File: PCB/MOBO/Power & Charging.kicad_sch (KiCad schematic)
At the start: 53 parts, among them J201 MAIN-USBC-OTG/PWR, Q201 AO3401A, Q202 FS8205A, Q203 IRLML6344, Q204 Si4435DDY, SW201 PCM12SMTR, U201 DW01A, U202 LC709203FQH-01TWG, U203 MCP73871-1AA, U204 TPS61230DRC

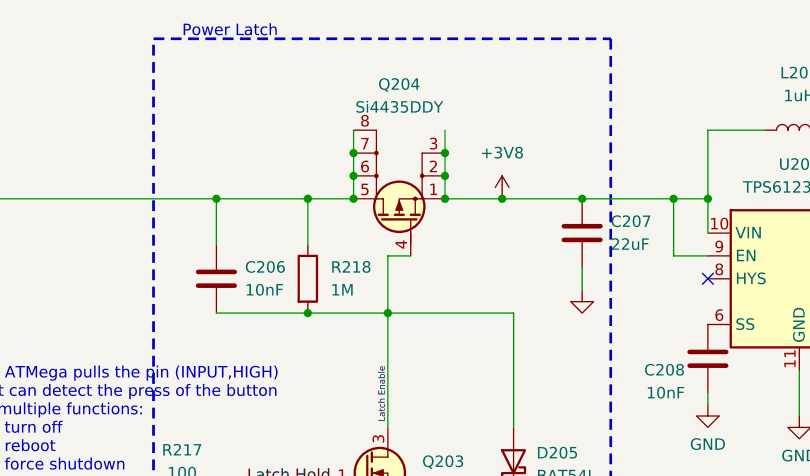
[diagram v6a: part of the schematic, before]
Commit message: replaced latching circuit PMOS
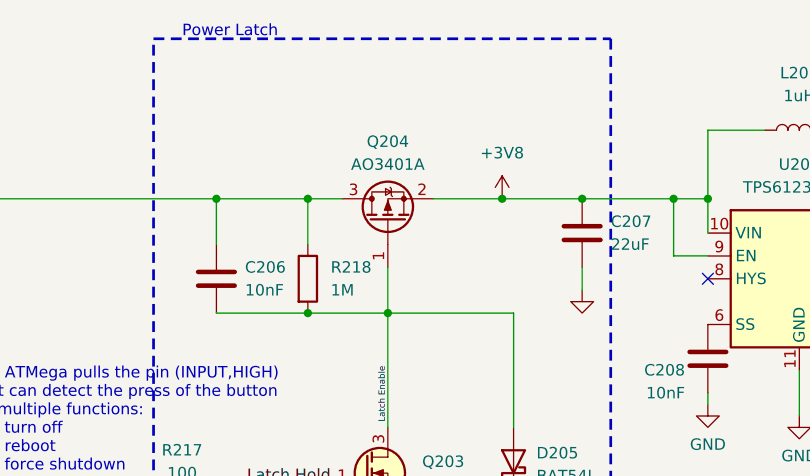
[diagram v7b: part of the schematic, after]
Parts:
- removed Q204: Si4435DDY, Package_SO:SOIC-8-1EP_3.9x4.9mm_P1.27mm_EP2.41x3.3mm, symbol PCM_Transistor_MOSFET_AKL:Si4435DDY
- added Q204: AO3401A, Package_TO_SOT_SMD:SOT-23, symbol Transistor_FET:AO3401A
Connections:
- net +3V8: now also Q204.2 (S)
- net Charger 3V8 out: now also Q204.3 (D)
- net Latch Enable: now also Q204.1 (G)
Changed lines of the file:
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@@
 	)
 	(junction
+		(at 252.73 36.83)
+		(diameter 0)
+		(color 0 0 0 0)
+	)
+	(junction
 		(at 340.36 43.18)
 		(diameter 0)
@@
 	)
 	(junction
-		(at 257.81 36.83)
-		(diameter 0)
-		(color 0 0 0 0)
-	)
-	(junction
 		(at 27.94 74.93)
 		(diameter 0)
@@
 	)
 	(junction
-		(at 274.32 36.83)
-		(diameter 0)
-		(color 0 0 0 0)
-	)
-	(junction
 		(at 63.5 36.83)
 		(diameter 0)
@@
 	)
 	(junction
-		(at 267.97 34.29)
-		(diameter 0)
-		(color 0 0 0 0)
-	)
-	(junction
 		(at 335.28 43.18)
 		(diameter 0)
@@
 	)
 	(junction
-		(at 267.97 36.83)
-		(diameter 0)
-		(color 0 0 0 0)
-	)
-	(junction
 		(at 242.57 36.83)
 		(diameter 0)
@@
 	)
 	(junction
-		(at 267.97 31.75)
-		(diameter 0)
-		(color 0 0 0 0)
-	)
-	(junction
 		(at 361.95 43.18)
 		(diameter 0)
@@
 	)
 	(junction
-		(at 257.81 31.75)
-		(diameter 0)
-		(color 0 0 0 0)
-	)
-	(junction
 		(at 134.62 96.52)
 		(diameter 0)
@@
 	)
 	(junction
-		(at 252.73 36.83)
-		(diameter 0)
-		(color 0 0 0 0)
-	)
-	(junction
 		(at 74.93 227.33)
 		(diameter 0)
@@
 	)
 	(junction
+		(at 274.32 36.83)
+		(diameter 0)
+		(color 0 0 0 0)
+	)
+	(junction
 		(at 260.35 85.09)
 		(diameter 0)
@@
 	)
 	(junction
-		(at 257.81 34.29)
-		(diameter 0)
-		(color 0 0 0 0)
-	)
-	(junction
 		(at 326.39 50.8)
 		(diameter 0)
@@
 	(wire
 		(pts
-			(xy 252.73 36.83) (xy 257.81 36.83)
-		)
-		(stroke
-			(width 0)
-			(type default)
-		)
-	)
-	(wire
-		(pts
 			(xy 62.23 36.83) (xy 63.5 36.83)
 		)
@@
 	(wire
 		(pts
-			(xy 261.62 43.18) (xy 261.62 49.53)
-		)
-		(stroke
-			(width 0)
-			(type default)
-		)
-	)
-	(wire
-		(pts
 			(xy 128.27 96.52) (xy 134.62 96.52)
 		)
@@
 	(wire
 		(pts
-			(xy 267.97 29.21) (xy 267.97 31.75)
-		)
-		(stroke
-			(width 0)
-			(type default)
-		)
-	)
-	(wire
-		(pts
 			(xy 127 41.91) (xy 127 44.45)
 		)
@@
 	(wire
 		(pts
-			(xy 257.81 31.75) (xy 257.81 34.29)
-		)
-		(stroke
-			(width 0)
-			(type default)
-		)
-	)
-	(wire
-		(pts
 			(xy 139.7 210.82) (xy 147.32 210.82)
 		)
@@
 	(wire
 		(pts
-			(xy 261.62 43.18) (xy 264.16 43.18)
-		)
-		(stroke
-			(width 0)
-			(type default)
-		)
-	)
-	(wire
-		(pts
 			(xy 119.38 36.83) (xy 137.16 36.83)
 		)
@@
 	(wire
 		(pts
-			(xy 252.73 68.58) (xy 252.73 71.12)
+			(xy 266.7 36.83) (xy 274.32 36.83)
 		)
 		(stroke
@@
 	(wire
 		(pts
-			(xy 317.5 29.21) (xy 317.5 40.64)
+			(xy 252.73 68.58) (xy 252.73 71.12)
 		)
 		(stroke
@@
 	(wire
 		(pts
-			(xy 119.38 218.44) (xy 129.54 218.44)
+			(xy 317.5 29.21) (xy 317.5 40.64)
 		)
 		(stroke
@@
 	(wire
 		(pts
-			(xy 261.62 49.53) (xy 275.59 49.53)
+			(xy 119.38 218.44) (xy 129.54 218.44)
 		)
 		(stroke
@@
 	(wire
 		(pts
-			(xy 109.22 51.435) (xy 115.57 51.435)
+			(xy 261.62 49.53) (xy 275.59 49.53)
 		)
 		(stroke
@@
 	(wire
 		(pts
-			(xy 297.18 59.69) (xy 297.18 58.42)
+			(xy 261.62 44.45) (xy 261.62 49.53)
 		)
 		(stroke
@@
 	(wire
 		(pts
-			(xy 283.21 36.83) (xy 293.37 36.83)
+			(xy 109.22 51.435) (xy 115.57 51.435)
 		)
 		(stroke
@@
 	(wire
 		(pts
-			(xy 110.49 254) (xy 53.34 254)
+			(xy 297.18 59.69) (xy 297.18 58.42)
 		)
 		(stroke
@@
 	(wire
 		(pts
-			(xy 260.35 85.09) (xy 275.59 85.09)
+			(xy 283.21 36.83) (xy 293.37 36.83)
 		)
 		(stroke
@@
 	(wire
 		(pts
-			(xy 173.99 44.45) (xy 184.15 44.45)
+			(xy 110.49 254) (xy 53.34 254)
 		)
 		(stroke
@@
 	(wire
 		(pts
-			(xy 246.38 68.58) (xy 252.73 68.58)
+			(xy 260.35 85.09) (xy 275.59 85.09)
 		)
 		(stroke
@@
 	(wire
 		(pts
-			(xy 297.18 29.21) (xy 297.18 36.83)
+			(xy 173.99 44.45) (xy 184.15 44.45)
 		)
 		(stroke
@@
 	(wire
 		(pts
-			(xy 267.97 34.29) (xy 267.97 36.83)
+			(xy 246.38 68.58) (xy 252.73 68.58)
 		)
 		(stroke
@@
 	(wire
 		(pts
-			(xy 267.97 31.75) (xy 267.97 34.29)
+			(xy 297.18 29.21) (xy 297.18 36.83)
 		)
 		(stroke
@@
 	(wire
 		(pts
-			(xy 257.81 29.21) (xy 257.81 31.75)
-		)
-		(stroke
-			(width 0)
-			(type default)
-		)
-	)
-	(wire
-		(pts
 			(xy 106.68 208.28) (xy 106.68 218.44)
 		)
@@
 	(wire
 		(pts
-			(xy 267.97 36.83) (xy 274.32 36.83)
-		)
-		(stroke
-			(width 0)
-			(type default)
-		)
-	)
-	(wire
-		(pts
 			(xy 335.28 68.58) (xy 335.28 43.18)
 		)
@@
 	(wire
 		(pts
-			(xy 257.81 34.29) (xy 257.81 36.83)
+			(xy 63.5 39.37) (xy 63.5 36.83)
 		)
 		(stroke
@@
 	(wire
 		(pts
-			(xy 63.5 39.37) (xy 63.5 36.83)
+			(xy 69.85 242.57) (xy 74.93 242.57)
 		)
 		(stroke
@@
 	(wire
 		(pts
-			(xy 69.85 242.57) (xy 74.93 242.57)
+			(xy 119.38 210.82) (xy 119.38 218.44)
 		)
 		(stroke
@@
 	(wire
 		(pts
-			(xy 119.38 210.82) (xy 119.38 218.44)
+			(xy 252.73 36.83) (xy 256.54 36.83)
 		)
 		(stroke
@@
 	)
 	(symbol
+		(lib_id "Transistor_FET:AO3401A")
+		(at 261.62 39.37 90)
+		(unit 1)
+		(exclude_from_sim no)
+		(in_bom yes)
+		(on_board yes)
+		(dnp no)
+		(fields_autoplaced yes)
+		(property "Reference" "Q204"
+			(at 261.62 30.48 90)
+			(effects
+				(font
+					(size 1.27 1.27)
+				)
+			)
+		)
+		(property "Value" "AO3401A"
+			(at 261.62 33.02 90)
+			(effects
+				(font
+					(size 1.27 1.27)
+				)
+			)
+		)
+		(property "Footprint" "Package_TO_SOT_SMD:SOT-23"
+			(at 263.525 34.29 0)
+			(effects
+				(font
+					(size 1.27 1.27)
+					(italic yes)
+				)
+				(justify left)
+				(hide yes)
+			)
+		)
+		(property "Datasheet" "http://www.aosmd.com/pdfs/datasheet/AO3401A.pdf"
+			(at 261.62 39.37 0)
+			(effects
+				(font
+					(size 1.27 1.27)
+				)
+				(justify left)
+				(hide yes)
+			)
+		)
+		(property "Description" ""
+			(at 261.62 39.37 0)
+			(effects
+				(font
+					(size 1.27 1.27)
+				)
+				(hide yes)
+			)
+		)
+		(pin "1"
+		)
+		(pin "3"
+		)
+		(pin "2"
+		)
+		(instances
+			(project "MOBO"
+				(path "/2d62a3c1-c4f2-4921-9f6b-8dc8aef69d64/968b581c-59b8-4e39-ae9d-82f589704db7"
+					(reference "Q204")
+					(unit 1)
+				)
+			)
+		)
+	)
+	(symbol
 		(lib_id "Device:R")
 		(at 115.57 57.15 0)
@@
 					(unit 1)
 				)
-			)
-		)
-	)
-	(symbol
-		(lib_id "PCM_Transistor_MOSFET_AKL:Si4435DDY")
-		(at 262.89 39.37 270)
-		(mirror x)
-		(unit 1)
-		(exclude_from_sim no)
-		(in_bom yes)
-		(on_board yes)
-		(dnp no)
-		(property "Reference" "Q204"
-			(at 262.89 24.13 90)
-			(effects
-				(font
-					(size 1.27 1.27)
-				)
-			)
-		)
-		(property "Value" "Si4435DDY"
-			(at 262.89 26.67 90)
-			(effects
-				(font
-					(size 1.27 1.27)
-				)
-			)
-		)
-		(property "Footprint" "Package_SO:SOIC-8-1EP_3.9x4.9mm_P1.27mm_EP2.41x3.3mm"
-			(at 260.35 34.29 0)
-			(effects
-				(font
-					(size 1.27 1.27)
-				)
-				(hide yes)
-			)
-		)
-		(property "Datasheet" "https://octopart.com/si4435ddy-t1-ge3-vishay-42674275?r=sp"
-			(at 262.89 39.37 0)
-			(effects
-				(font
-					(size 1.27 1.27)
-				)
-				(hide yes)
-			)
-		)
-		(property "Description" ""
-			(at 262.89 39.37 0)
-			(effects
-				(font
-					(size 1.27 1.27)
-				)
-				(hide yes)
-			)
-		)
-		(pin "5"
-		)
-		(pin "4"
-		)
-		(pin "6"
-		)
-		(pin "7"
-		)
-		(pin "2"
-		)
-		(pin "3"
-		)
-		(pin "8"
-		)
-		(pin "1"
-		)
-		(instances
-			(project "MOBO"
-				(path "/2d62a3c1-c4f2-4921-9f6b-8dc8aef69d64/968b581c-59b8-4e39-ae9d-82f589704db7"
-					(reference "Q204")
-					(unit 1)
-				)

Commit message: fix: battery charging protection module
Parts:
- removed C201: 100nF, Capacitor_SMD:C_0805_2012Metric, symbol Device:C
- removed C203: 1uF, Capacitor_SMD:C_0805_2012Metric, symbol Device:C
- removed Q202: FS8205A, FS8205A:SOP65P640X120-8N, symbol FS8205A:FS8205A
- removed R202, R213: 100, Resistor_SMD:R_0805_2012Metric, symbol Device:R
- removed R211: 1k, Resistor_SMD:R_0805_2012Metric, symbol Device:R
- removed R212: 10k, Resistor_SMD:R_0805_2012Metric, symbol Device:R
- removed TH202: NCU18XH103F6SRB, Capacitor_SMD:C_0603_1608Metric, symbol Device:Thermistor_NTC
- removed U201: DW01A, DW01A:SOT23-6, symbol DW01A:DW01A
- removed U202: LC709203FQH-01TWG, Package_DFN_QFN:WDFN-8-1EP_4x3mm_P0.65mm_EP2.4x1.8mm, symbol Battery_Management:LC709203FQH-01TWG
- added U1: MAX17261xxTD, Package_DFN_QFN:TDFN-14-1EP_3x3mm_P0.4mm_EP1.78x2.35mm, symbol Battery_Management:MAX17261xxTD
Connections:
- new net: U1.15 (GND), U1.8 (GND)
- no-connect marks 6 -> 3
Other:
- note removed: "Just noticed that the battery has the protection circuit so maybe all this can create a redundancy and a problem?"
- note removed: "To be reviewed"
